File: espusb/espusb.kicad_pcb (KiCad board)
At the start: 2 copper layers, 61 x 18.4 mm, 27 parts, among them CON1 SD_Card, P1 USB_A, P4 CONN_02X04, P5 CONN_01X03, U1 MCP1603, U2 FT232, U3 esp8266, U4 SERFLASH, X1 CRYSTAL_SMD

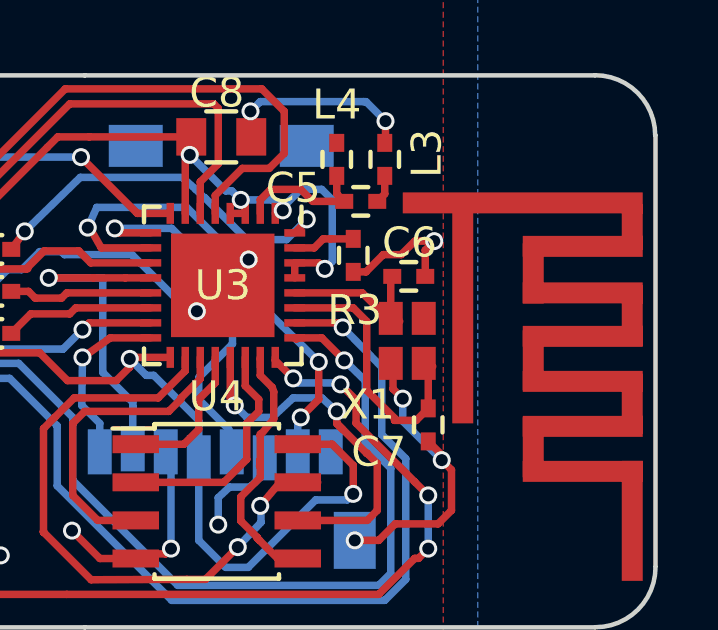
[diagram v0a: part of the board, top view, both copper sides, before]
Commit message: missing link to antenna and ground
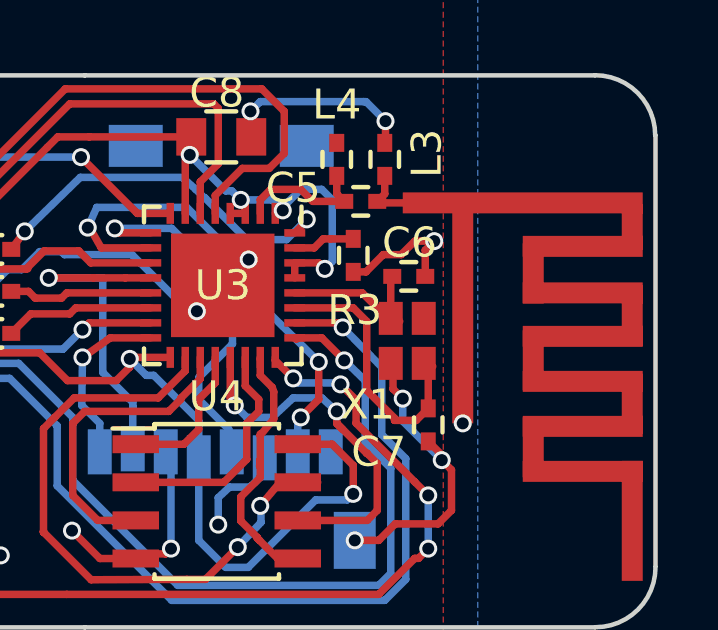
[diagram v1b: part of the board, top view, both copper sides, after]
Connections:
- A1 pad 2: (no net) -> GND
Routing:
- net Net-(A1-Pad1): track 0.95 -> 5.82 mm
- net GND: track 49.1 -> 52.6 mm, vias 14 -> 15
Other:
- board text added: "espusb r5 Whiteford Research"
- board text removed: "espusb r4 Whiteford Research"
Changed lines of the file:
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@@
 (kicad_pcb (version 4) (host pcbnew "(2015-11-24 BZR 6329)-product")
   (general
-    (links 103)
-    (no_connects 14)
-    (area 121.924999 95.024999 190.475001 114.575001)
+    (links 104)
+    (no_connects 13)
+    (area 121.924999 96.719999 183.100001 115.275001)
     (thickness 1.6)
     (drawings 11)
-    (tracks 537)
+    (tracks 541)
     (zones 0)
     (modules 27)
@@
     (pad 1 smd rect (at 3.65 8.65) (size 0.7 4) (layers F.Cu F.Paste F.Mask)
       (net 12 "Net-(A1-Pad1)"))
-    (pad 2 smd rect (at -2 1.9) (size 0.7 7) (layers F.Cu F.Paste F.Mask))
+    (pad 2 smd rect (at -2 1.9) (size 0.7 7) (layers F.Cu F.Paste F.Mask)
+      (net 2 GND))
   )
   (module Capacitors_SMD:C_0402 (layer F.Cu)
@@
   (gr_line (start 164 96.8) (end 181 96.8) (angle 90) (layer Edge.Cuts) (width 0.15))
   (gr_line (start 122 98.8) (end 122 113.2) (angle 90) (layer Edge.Cuts) (width 0.15))
-  (gr_text "espusb r4\nWhiteford Research" (at 142 105) (layer B.SilkS)
+  (gr_text "espusb r5\nWhiteford Research" (at 142 105) (layer B.SilkS)
     (effects (font (size 1.5 1.5) (thickness 0.3)) (justify mirror))
   )
@@
   (segment (start 144.4 106.45) (end 144.65 106.7) (width 0.25) (layer F.Cu) (net 1))
   (segment (start 144.65 106.7) (end 146.4 106.7) (width 0.25) (layer F.Cu) (net 1))
+  (segment (start 176.6 104.9) (end 176.6 108.4) (width 0.25) (layer F.Cu) (net 2) (status C00000))
+  (via (at 176.6 108.4) (size 0.6) (drill 0.4) (layers F.Cu B.Cu) (net 2) (status C00000))
   (segment (start 172.95 103.35) (end 173.375 103.35) (width 0.25) (layer F.Cu) (net 2))
   (segment (start 175.35 102.625) (end 175.65 102.325) (width 0.25) (layer F.Cu) (net 2))
@@
   (segment (start 140 99.7) (end 139.425 100.275) (width 0.25) (layer F.Cu) (net 11))
   (segment (start 139.425 101.8) (end 139.425 100.275) (width 0.25) (layer F.Cu) (net 11))
+  (segment (start 178.6 101.05) (end 173.8 101.05) (width 0.25) (layer F.Cu) (net 12) (status C00000))
+  (segment (start 173.8 101.05) (end 173.75 101) (width 0.25) (layer F.Cu) (net 12) (status C00000))
   (segment (start 174 100.15) (end 174 100.75) (width 0.25) (layer F.Cu) (net 12))
   (segment (start 174 100.75) (end 173.75 101) (width 0.25) (layer F.Cu) (net 12))

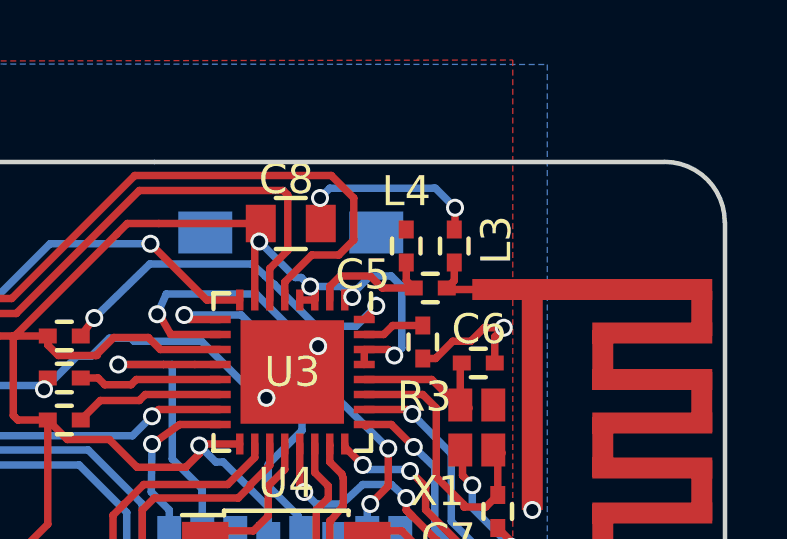
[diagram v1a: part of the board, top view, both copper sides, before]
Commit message: made track thicker
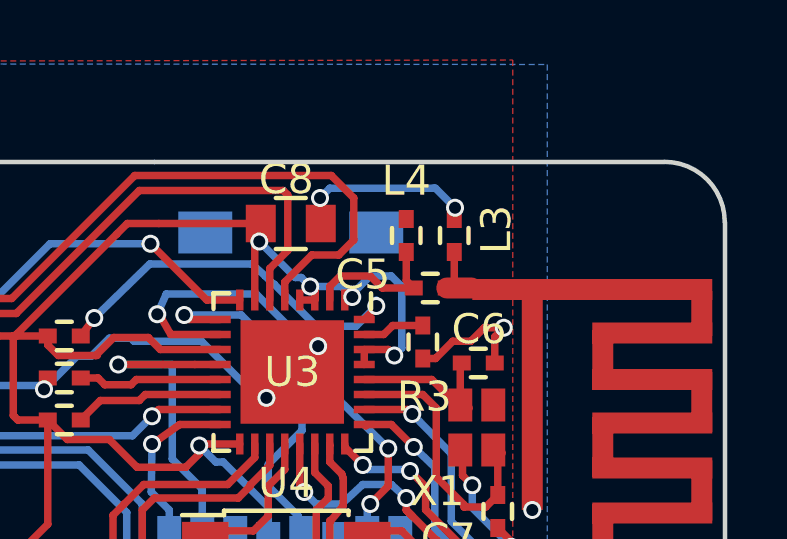
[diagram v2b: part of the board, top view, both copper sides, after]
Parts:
- moved L3 0.35 mm to (174.0, 99.2)
- moved L4 0.35 mm to (172.4, 99.2)
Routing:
- net Net-(A1-Pad1): track 5.82 -> 7.07 mm
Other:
- net class antenna added: clearance 0.01, trace_width 0.7, via_dia 0.6, via_drill 0.4
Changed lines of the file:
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@@
     (links 104)
     (no_connects 13)
-    (area 121.924999 96.719999 183.100001 115.275001)
+    (area 120.874999 91.475 189.22262 118.550001)
     (thickness 1.6)
     (drawings 11)
-    (tracks 541)
+    (tracks 543)
     (zones 0)
     (modules 27)
@@
   (layers
     (0 F.Cu signal)
-    (31 B.Cu signal)
+    (31 B.Cu signal hide)
     (32 B.Adhes user)
     (33 F.Adhes user)
@@
     (add_net USB_DP)
   )
+  (net_class antenna ""
+    (clearance 0.01)
+    (trace_width 0.7)
+    (via_dia 0.6)
+    (via_drill 0.4)
+    (uvia_dia 0.3)
+    (uvia_drill 0.1)
+  )
   (module espusb:SSOP-28_5.3x10.2mm_Pitch0.65mm (layer F.Cu)
     (at 137.8 105.4 270)
@@
   )
   (module Capacitors_SMD:C_0402 (layer F.Cu)
-    (at 174 99.6 90)
+    (at 174 99.25 90)
     (descr "Capacitor SMD 0402, reflow soldering, AVX (see smccp.pdf)")
     (tags "capacitor 0402")
@@
   )
   (module Capacitors_SMD:C_0402 (layer F.Cu)
-    (at 172.4 99.6 90)
+    (at 172.4 99.25 90)
     (descr "Capacitor SMD 0402, reflow soldering, AVX (see smccp.pdf)")
     (tags "capacitor 0402")
@@
   (segment (start 144.4 106.45) (end 144.65 106.7) (width 0.25) (layer F.Cu) (net 1))
   (segment (start 144.65 106.7) (end 146.4 106.7) (width 0.25) (layer F.Cu) (net 1))
-  (segment (start 176.6 104.9) (end 176.6 108.4) (width 0.25) (layer F.Cu) (net 2) (status C00000))
-  (via (at 176.6 108.4) (size 0.6) (drill 0.4) (layers F.Cu B.Cu) (net 2) (status C00000))
+  (segment (start 176.6 104.9) (end 176.6 108.4) (width 0.25) (layer F.Cu) (net 2))
+  (via (at 176.6 108.4) (size 0.6) (drill 0.4) (layers F.Cu B.Cu) (net 2))
   (segment (start 172.95 103.35) (end 173.375 103.35) (width 0.25) (layer F.Cu) (net 2))
   (segment (start 175.35 102.625) (end 175.65 102.325) (width 0.25) (layer F.Cu) (net 2))
@@
   (segment (start 166.875 109.525) (end 166.7 109.35) (width 0.25) (layer B.Cu) (net 2))
   (segment (start 169.525 98) (end 169.85 97.675) (width 0.25) (layer B.Cu) (net 2))
-  (segment (start 174.025 98.325) (end 174.025 99.025) (width 0.25) (layer F.Cu) (net 2))
+  (segment (start 174.025 98.325) (end 174.025 98.675) (width 0.25) (layer F.Cu) (net 2) (status 20))
   (via (at 174.025 98.325) (size 0.6) (drill 0.4) (layers F.Cu B.Cu) (net 2))
   (segment (start 173.375 97.675) (end 174.025 98.325) (width 0.25) (layer B.Cu) (net 2))
   (segment (start 173.3 97.675) (end 173.375 97.675) (width 0.25) (layer B.Cu) (net 2))
   (segment (start 169.85 97.675) (end 173.3 97.675) (width 0.25) (layer B.Cu) (net 2))
-  (segment (start 174.025 99.025) (end 174 99.05) (width 0.25) (layer F.Cu) (net 2))
+  (segment (start 174.025 98.675) (end 174 98.7) (width 0.25) (layer F.Cu) (net 2) (status 30))
   (segment (start 169.55 98.85) (end 169.525 98.825) (width 0.25) (layer F.Cu) (net 2))
   (segment (start 169.525 98.825) (end 169.525 98) (width 0.25) (layer F.Cu) (net 2))
@@
   (segment (start 140 99.7) (end 139.425 100.275) (width 0.25) (layer F.Cu) (net 11))
   (segment (start 139.425 101.8) (end 139.425 100.275) (width 0.25) (layer F.Cu) (net 11))
+  (segment (start 174 99.8) (end 174 100.75) (width 0.25) (layer F.Cu) (net 12) (status C00000))
+  (segment (start 174 100.75) (end 173.75 101) (width 0.25) (layer F.Cu) (net 12) (status C00000))
   (segment (start 178.6 101.05) (end 173.8 101.05) (width 0.25) (layer F.Cu) (net 12) (status C00000))
   (segment (start 173.8 101.05) (end 173.75 101) (width 0.25) (layer F.Cu) (net 12) (status C00000))
-  (segment (start 174 100.15) (end 174 100.75) (width 0.25) (layer F.Cu) (net 12))
-  (segment (start 174 100.75) (end 173.75 101) (width 0.25) (layer F.Cu) (net 12))
-  (segment (start 172.4 100.15) (end 172.4 100.75) (width 0.25) (layer F.Cu) (net 13))
+  (segment (start 173.75 101) (end 174.575 101) (width 0.7) (layer F.Cu) (net 12) (status 400000))
+  (segment (start 173.8 101.05) (end 173.75 101) (width 0.25) (layer F.Cu) (net 12))
+  (segment (start 172.4 99.8) (end 172.4 100.75) (width 0.25) (layer F.Cu) (net 13) (status 10))
   (segment (start 172.4 100.75) (end 172.65 101) (width 0.25) (layer F.Cu) (net 13))
   (segment (start 172.65 101) (end 171.6 101) (width 0.25) (layer F.Cu) (net 13))

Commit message: r6 version (with ch340)
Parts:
- removed L2: bead 0805, Resistors_SMD:R_0805_HandSoldering
- added C9: 100nF, Capacitors_SMD:C_0805, F.Cu at (140.3, 100.0)
- added Y1: 12MHz, Crystals:HC-49V, F.Cu at (138.8, 112.0)
- C3: value 10nF -> 22pF; footprint Resistors_SMD:R_0603_HandSoldering -> Capacitors_SMD:C_0603
- C4: value 100nF -> 22pF; footprint Resistors_SMD:R_0603_HandSoldering -> Capacitors_SMD:C_0603
- U2: value FT232 -> ch340; footprint espusb:SSOP-28_5.3x10.2mm_Pitch0.65mm -> SMD_Packages:SO-16-N
- moved C4 6.95 mm to (129.3, 111.2), turned to 90 degrees
- moved JP1 5.90 mm to (140.5, 106.7), turned to 90 degrees
- moved C3 4.69 mm to (143.2, 111.2), turned to 90 degrees
- moved U2 3.99 mm to (134.3, 103.5)
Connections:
- C3 pad 1: +5V -> Net-(C3-Pad1)
- JP1 pad 1: Net-(JP1-Pad1) -> +3V3
- JP1 pad 2: Net-(JP1-Pad2) -> Net-(C9-Pad1)
- U2 pad 1: FT232_TX -> GND
- U2 pad 15: USB_DP -> (no net)
- U2 pad 16: USB_DM -> Net-(C9-Pad1)
- U2 pad 2: (no net) -> FT232_TX
- U2 pad 3: (no net) -> FT232_RX
- U2 pad 4: Net-(C4-Pad1) -> Net-(C9-Pad1)
- U2 pad 5: FT232_RX -> USB_DP
- U2 pad 6: (no net) -> USB_DM
- U2 pad 7: GND -> Net-(C3-Pad1)
- U2 pad 8: (no net) -> Net-(C4-Pad1)
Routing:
- net +3V3: track 85.9 -> 105.9 mm
- net Net-(C9-Pad1): track 0.00 -> 17.7 mm
- net Net-(C3-Pad1): track 0.00 -> 14.2 mm
- net FT232_TX: track 50.8 -> 62.9 mm
- net FT232_RX: track 56.1 -> 64.5 mm
- net Net-(JP1-Pad2): track 5.40 -> 0.00 mm
- net USB_DM: track 10.4 -> 5.08 mm
- net USB_DP: track 9.30 -> 4.77 mm
- net Net-(C4-Pad1): track 13.5 -> 9.56 mm
- net Net-(JP1-Pad1): track 3.80 -> 0.00 mm
- net +5V: track 31.3 -> 32.3 mm
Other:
- board text added: "espusb r6 Whiteford Research"
- board text removed: "espusb r5 Whiteford Research"

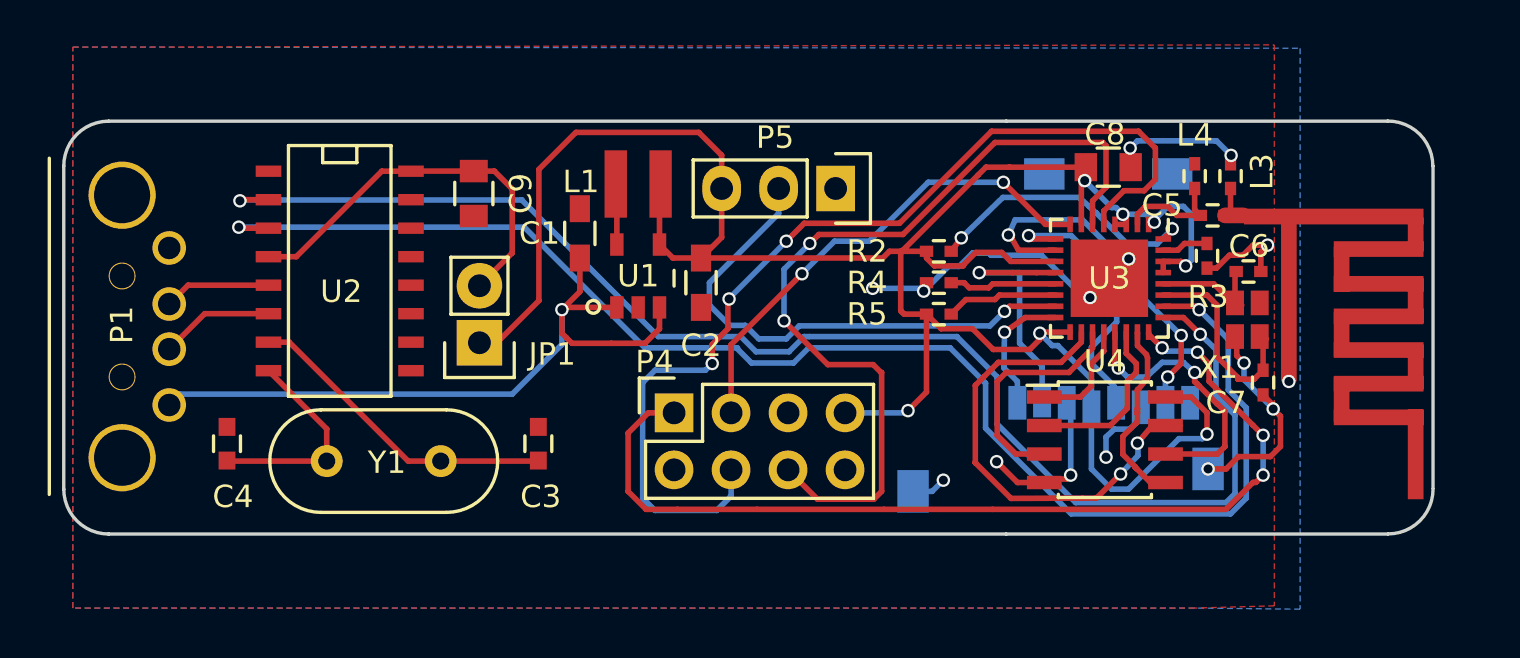
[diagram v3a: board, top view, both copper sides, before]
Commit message: updated microsd footprint and relaid board
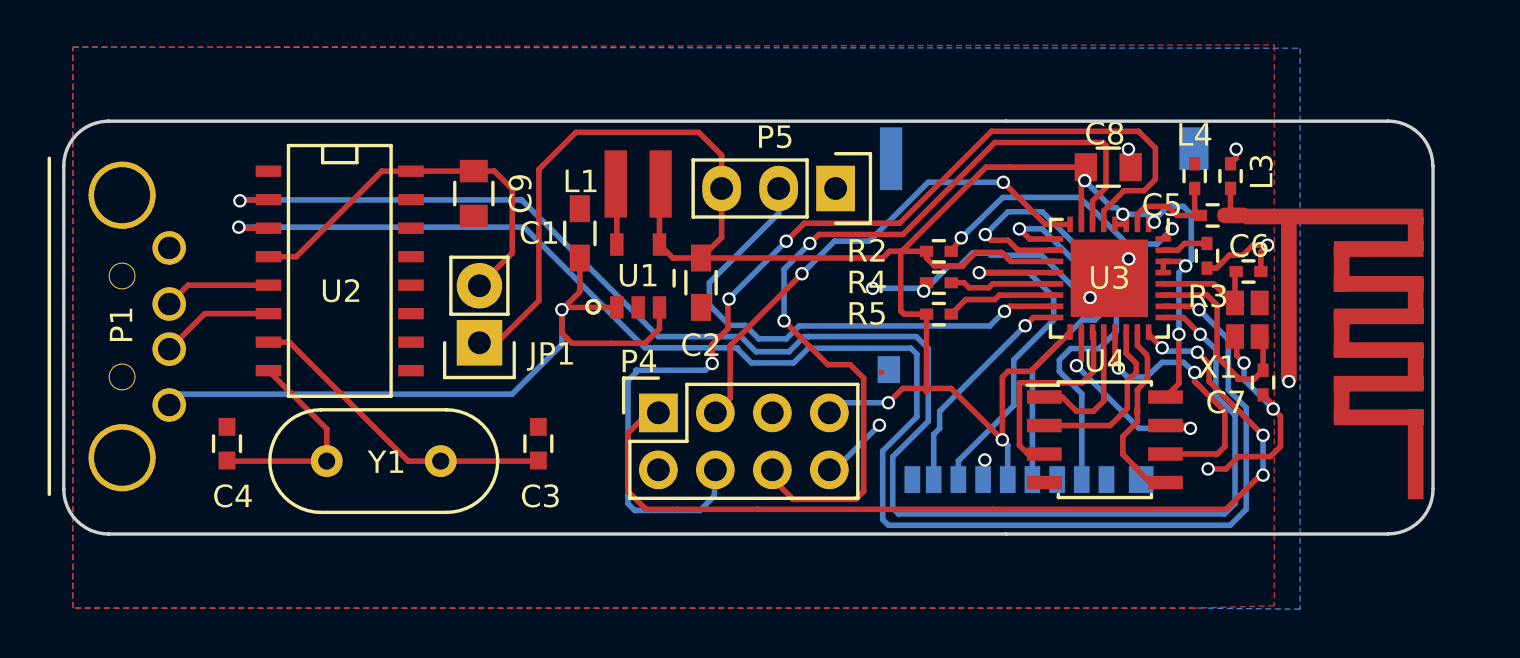
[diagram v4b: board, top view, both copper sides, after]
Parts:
- moved CON1 1.39 mm to (166.4, 109.5)
- moved P4 0.70 mm to (148.5, 109.8)
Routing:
- net GND: track 52.3 -> 39.2 mm, vias 15 -> 13
- net F_HOLD: track 21.0 -> 10.2 mm
- net FT232_RX: track 64.5 -> 70.6 mm
- net FT232_TX: track 62.9 -> 68.8 mm
- net MTCK: track 11.4 -> 17.1 mm
- net MTDI: track 16.7 -> 21.9 mm, vias 3 -> 1
- net MTMS: track 12.4 -> 16.9 mm
- net GPIO4: track 5.77 -> 10.1 mm
- net +3V3: track 105.9 -> 101.7 mm
- net F_CS: track 5.54 -> 6.78 mm
- net F_WP: track 10.4 -> 9.34 mm
- net Net-(P4-Pad4): track 44.7 -> 45.5 mm
- net Net-(P4-Pad6): track 38.3 -> 37.5 mm
- net CON1: track 43.5 -> 42.8 mm

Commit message: current version
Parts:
- added C10: 10uF, Capacitors_SMD:C_0805, F.Cu at (161.8, 110.7)
- added R1: 10K, Resistors_SMD:R_0603, F.Cu at (162.1, 109.5)
- added REF**: 1pin, Connect:1pin, F.Cu at (179.0, 98.5)
- added REF**: 1pin, Connect:1pin, F.Cu at (179.0, 113.5)
- added REF**: 1pin, Connect:1pin, F.Cu at (127.5, 113.5)
- added REF**: 1pin, Connect:1pin, F.Cu at (127.5, 98.5)
- moved R3 1.94 mm to (174.8, 102.2), turned to 180 degrees
- moved A1 1.53 mm to (180.1, 102.6)
- moved C5 0.36 mm to (173.2, 100.6)
- moved C8 0.08 mm to (168.6, 98.8), turned to 180 degrees
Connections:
- CON1 pad 1: GPIO4 -> (no net)
- CON1 pad 2: MTCK -> GPIO4
- CON1 pad 3: GND -> MTCK
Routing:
- net +3V3: track 101.7 -> 113.2 mm, vias 7 -> 9
- net GND: track 39.2 -> 29.7 mm, vias 13 -> 12
- net Net-(P4-Pad4): track 45.5 -> 42.1 mm
- net Net-(P4-Pad6): track 37.5 -> 34.4 mm
- net F_DI: track 8.88 -> 11.6 mm, vias 0 -> 2
- net F_CLK: track 12.6 -> 9.87 mm
- net MTCK: track 17.1 -> 14.4 mm, vias 1 -> 3
- net MTMS: track 16.9 -> 14.3 mm
- net GPIO4: track 10.1 -> 8.33 mm
- net Net-(R3-Pad2): track 2.07 -> 3.39 mm
- net F_WP: track 9.34 -> 8.45 mm, vias 0 -> 2
- net Net-(R2-Pad2): track 12.9 -> 13.6 mm
- net F_D0: track 8.50 -> 7.83 mm
- net F_HOLD: track 10.2 -> 9.66 mm
- net Net-(P5-Pad2): track 23.1 -> 23.7 mm
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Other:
- board size 61 x 18.4 mm -> 62.8 x 18.4 mm
- board text added: "espusb r12 Whiteford Research"
- board text removed: "espusb r6 Whiteford Research"

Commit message: misssing files
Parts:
- removed A1: antenna, wifiantenna:wifi_antenna
- added svg2mod: G***, antenna:svg2mod, F.Cu at (176.8, 105.9)
- moved L4 1.07 mm to (173.4, 99.0)
- moved C5 0.86 mm to (173.9, 100.2)
- moved L3 0.69 mm to (174.6, 99.0)
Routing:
- net GND: track 29.7 -> 22.2 mm, vias 12 -> 11
- net Net-(C5-Pad1): track 4.82 -> 0.45 mm
- net Net-(A1-Pad1): track 6.88 -> 10.0 mm, vias 0 -> 1
- net F_DI: track 11.6 -> 10.4 mm
